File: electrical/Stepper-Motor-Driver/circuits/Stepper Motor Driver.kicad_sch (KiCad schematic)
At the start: 19 parts, among them J1 Conn_01x24_Socket, J2 Conn_01x24_Socket, J3 Screw_Terminal_01x04

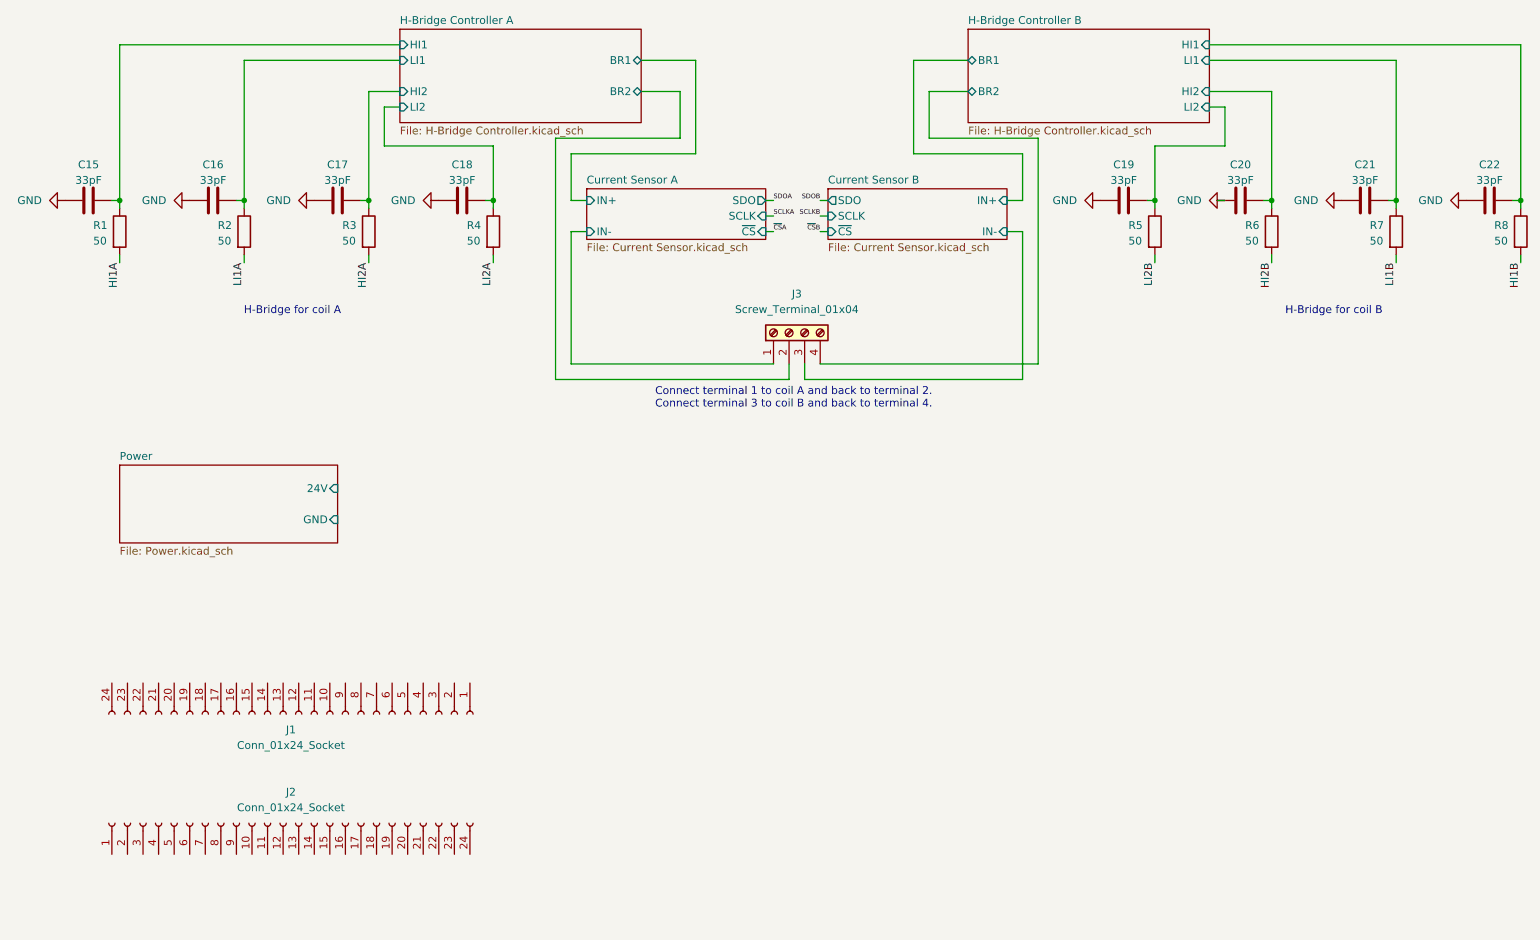
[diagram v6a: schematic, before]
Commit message: Adding Tang Nano 9k development board symbol and footprint
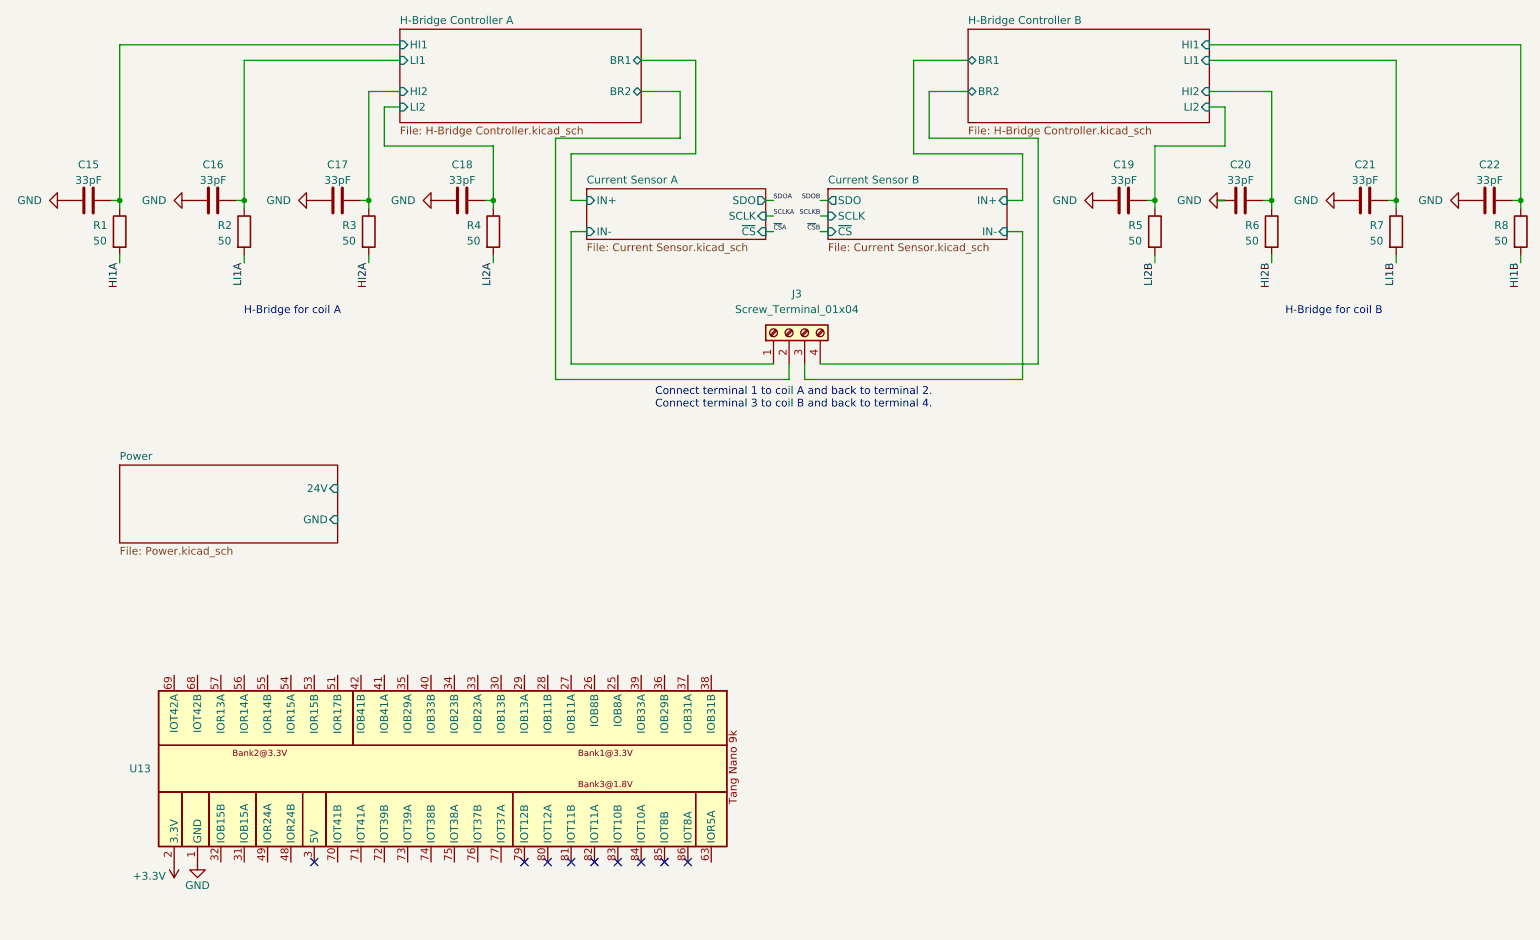
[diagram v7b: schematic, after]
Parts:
- removed J1, J2: Conn_01x24_Socket, Connector_PinHeader_2.54mm:PinHeader_1x27_P2.54mm_Vertical, symbol Connector:Conn_01x24_Socket
- added U13: (no value), Tang Nano 9k:Tang Nano 9k Header Pins, symbol Tang Nano 9k:Tang_Nano_9k
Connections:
- net GND: now also U13.1 (GND)
- new net +3.3V: U13.2 (3.3V)
- no-connect marks 0 -> 9

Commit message: Adding pin assignment for FPGA
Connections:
- net HI1A: now also U13.38 (IOB31B)
- net HI1B: now also U13.28 (IOB11B)
- net HI2A: now also U13.36 (IOB29B)
- net HI2B: now also U13.26 (IOB8B)
- net LI1A: now also U13.37 (IOB31A)
- net LI1B: now also U13.27 (IOB11A)
- net LI2A: now also U13.39 (IOB33A)
- net LI2B: now also U13.25 (IOB8A)
- net SCLKA: now also U13.30 (IOB13B)
- net SCLKB: now also U13.40 (IOB33B)
- net SDOA: now also U13.29 (IOB13A)
- net SDOB: now also U13.34 (IOB23B)
- net ~{CS}A: now also U13.33 (IOB23A)
- net ~{CS}B: now also U13.35 (IOB29A)
- net STEP: now reaches U13.70 (IOT41B)
- net DIR: now reaches U13.71 (IOT41A)
- net MICROSTEP_BIT1: now reaches U13.72 (IOT39B)
- net MICROSTEP_BIT2: now reaches U13.73 (IOT39A)
- net MICROSTEP_BIT3: now reaches U13.74 (IOT38B)
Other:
- moved on the sheet: U13
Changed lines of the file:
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@@
 	)
 	(no_connect
-		(at 101.6 162.56)
+		(at 63.5 137.16)
 	)
 	(no_connect
-		(at 105.41 162.56)
+		(at 59.69 137.16)
 	)
 	(no_connect
-		(at 120.65 162.56)
+		(at 44.45 137.16)
 	)
 	(no_connect
-		(at 124.46 162.56)
+		(at 40.64 137.16)
 	)
 	(no_connect
-		(at 97.79 162.56)
+		(at 67.31 137.16)
 	)
 	(no_connect
-		(at 63.5 162.56)
+		(at 101.6 137.16)
 	)
 	(no_connect
-		(at 116.84 162.56)
+		(at 48.26 137.16)
 	)
 	(no_connect
-		(at 113.03 162.56)
+		(at 52.07 137.16)
 	)
 	(no_connect
-		(at 109.22 162.56)
+		(at 55.88 137.16)
 	)
 	(wire
@@
 		)
 	)
+	(label "DIR"
+		(at 93.98 137.16 90)
+		(effects
+			(font
+				(size 1.27 1.27)
+			)
+			(justify left bottom)
+		)
+	)
+	(label "SCLKA"
+		(at 71.12 167.64 270)
+		(effects
+			(font
+				(size 0.762 0.762)
+			)
+			(justify right bottom)
+		)
+	)
+	(label "HI1A"
+		(at 36.83 167.64 270)
+		(effects
+			(font
+				(size 1.27 1.27)
+			)
+			(justify right bottom)
+		)
+	)
 	(label "HI2B"
 		(at 219.71 64.77 270)
@@
 		)
 	)
+	(label "MICROSTEP_BIT3"
+		(at 82.55 137.16 90)
+		(effects
+			(font
+				(size 1.27 1.27)
+			)
+			(justify left bottom)
+		)
+	)
+	(label "LI2B"
+		(at 52.07 167.64 270)
+		(effects
+			(font
+				(size 1.27 1.27)
+			)
+			(justify right bottom)
+		)
+	)
 	(label "SDOA"
 		(at 138.43 54.61 0)
@@
 	)
 	(label "~{CS}A"
+		(at 74.93 167.64 270)
+		(effects
+			(font
+				(size 0.762 0.762)
+			)
+			(justify right bottom)
+		)
+	)
+	(label "~{CS}A"
 		(at 138.43 59.69 0)
 		(effects
@@
 		)
 	)
+	(label "HI2B"
+		(at 55.88 167.64 270)
+		(effects
+			(font
+				(size 1.27 1.27)
+			)
+			(justify right bottom)
+		)
+	)
+	(label "~{CS}B"
+		(at 86.36 167.64 270)
+		(effects
+			(font
+				(size 0.762 0.762)
+			)
+			(justify right bottom)
+		)
+	)
 	(label "SDOB"
 		(at 146.05 54.61 180)
@@
 		)
 	)
+	(label "SDOB"
+		(at 78.74 167.64 270)
+		(effects
+			(font
+				(size 0.762 0.762)
+			)
+			(justify right bottom)
+		)
+	)
+	(label "MICROSTEP_BIT2"
+		(at 86.36 137.16 90)
+		(effects
+			(font
+				(size 1.27 1.27)
+			)
+			(justify left bottom)
+		)
+	)
 	(label "LI1B"
 		(at 240.03 64.77 270)
@@
 		)
 	)
+	(label "MICROSTEP_BIT1"
+		(at 90.17 137.16 90)
+		(effects
+			(font
+				(size 1.27 1.27)
+			)
+			(justify left bottom)
+		)
+	)
+	(label "STEP"
+		(at 97.79 137.16 90)
+		(effects
+			(font
+				(size 1.27 1.27)
+			)
+			(justify left bottom)
+		)
+	)
+	(label "LI1B"
+		(at 59.69 167.64 270)
+		(effects
+			(font
+				(size 1.27 1.27)
+			)
+			(justify right bottom)
+		)
+	)
+	(label "LI1A"
+		(at 40.64 167.64 270)
+		(effects
+			(font
+				(size 1.27 1.27)
+			)
+			(justify right bottom)
+		)
+	)
 	(label "HI1B"
 		(at 260.35 64.77 270)
@@
 		)
 	)
+	(label "SDOA"
+		(at 67.31 167.64 270)
+		(effects
+			(font
+				(size 0.762 0.762)
+			)
+			(justify right bottom)
+		)
+	)
+	(label "LI2A"
+		(at 48.26 167.64 270)
+		(effects
+			(font
+				(size 1.27 1.27)
+			)
+			(justify right bottom)
+		)
+	)
+	(label "HI2A"
+		(at 44.45 167.64 270)
+		(effects
+			(font
+				(size 1.27 1.27)
+			)
+			(justify right bottom)
+		)
+	)
+	(label "SCLKB"
+		(at 82.55 167.64 270)
+		(effects
+			(font
+				(size 0.762 0.762)
+			)
+			(justify right bottom)
+		)
+	)
+	(label "HI1B"
+		(at 63.5 167.64 270)
+		(effects
+			(font
+				(size 1.27 1.27)
+			)
+			(justify right bottom)
+		)
+	)
 	(symbol
 		(lib_id "power:GND")
@@
 	(symbol
 		(lib_id "power:+3.3V")
-		(at 40.64 162.56 180)
+		(at 124.46 137.16 0)
 		(unit 1)
 		(body_style 1)
@@
 		(dnp no)
 		(property "Reference" "#PWR077"
-			(at 40.64 158.75 0)
+			(at 124.46 140.97 0)
 			(hide yes)
 			(show_name no)
@@
 		)
 		(property "Value" "+3.3V"
-			(at 36.576 164.846 0)
+			(at 128.524 134.874 0)
 			(show_name no)
 			(do_not_autoplace no)
@@
 		)
 		(property "Footprint" ""
-			(at 40.64 162.56 0)
+			(at 124.46 137.16 0)
 			(hide yes)
 			(show_name no)
@@
 		)
 		(property "Datasheet" ""
-			(at 40.64 162.56 0)
+			(at 124.46 137.16 0)
 			(hide yes)
 			(show_name no)
@@
 		)
 		(property "Description" "Power symbol creates a global label with name \"+3.3V\""
-			(at 40.64 162.56 0)
+			(at 124.46 137.16 0)
 			(hide yes)
 			(show_name no)
@@
 	(symbol
 		(lib_id "power:GND")
-		(at 44.45 162.56 0)
+		(at 120.65 137.16 180)
 		(unit 1)
 		(body_style 1)
@@
 		(dnp no)
 		(property "Reference" "#PWR076"
-			(at 44.45 168.91 0)
+			(at 120.65 130.81 0)
 			(hide yes)
 			(show_name no)
@@
 		)
 		(property "Value" "GND"
-			(at 44.45 166.37 0)
+			(at 120.65 133.35 0)
 			(show_name no)
 			(do_not_autoplace no)
@@
 		)
 		(property "Footprint" ""
-			(at 44.45 162.56 0)
+			(at 120.65 137.16 0)
 			(hide yes)
 			(show_name no)
@@
 		)
 		(property "Datasheet" ""
-			(at 44.45 162.56 0)
+			(at 120.65 137.16 0)
 			(hide yes)
 			(show_name no)
@@
 		)
 		(property "Description" "Power symbol creates a global label with name \"GND\" , ground"
-			(at 44.45 162.56 0)
+			(at 120.65 137.16 0)
 			(hide yes)
 			(show_name no)
@@
 	(symbol
 		(lib_id "Tang Nano 9k:Tang_Nano_9k")
-		(at 130.81 134.62 270)
+		(at 34.29 165.1 90)
 		(unit 1)
 		(body_style 1)
@@
 		(dnp no)
 		(property "Reference" "U13"
-			(at 36.83 147.3199 90)
+			(at 128.27 152.4001 90)
 			(show_name no)
 			(do_not_autoplace no)
@@
 		)
 		(property "Value" ""
-			(at 130.81 134.62 0)
+			(at 34.29 165.1 0)
 			(show_name no)
 			(do_not_autoplace no)
@@
 		)
 		(property "Footprint" "Tang Nano 9k:Tang Nano 9k Header Pins"
-			(at 130.81 134.62 0)
+			(at 34.29 165.1 0)
 			(hide yes)
 			(show_name no)
@@
 		)
 		(property "Datasheet" ""
-			(at 130.81 134.62 0)
+			(at 34.29 165.1 0)
 			(hide yes)
 			(show_name no)
@@
 		)
 		(property "Description" ""
-			(at 130.81 134.62 0)
+			(at 34.29 165.1 0)
 			(hide yes)
 			(show_name no)
@@
 		)
 		(pin "24V" input
-			(at 67.31 101.6 0)
+			(at 31.75 101.6 180)
 			(effects
 				(font
 					(size 1.27 1.27)
 				)
-				(justify right)
+				(justify left)
 			)
 		)
 		(pin "GND" input
-			(at 67.31 106.68 0)
+			(at 31.75 106.68 180)
 			(effects
 				(font
 					(size 1.27 1.27)
 				)
-				(justify right)
+				(justify left)
 			)
 		)
